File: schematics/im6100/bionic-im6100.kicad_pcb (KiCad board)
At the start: 2 copper layers, 48.3 x 71.1 mm, 10 parts, among them J1 Bionic-P135, J2 Bionic-P245, U1 IM6100, U2 74HCT126, U3 11AA010-I/TO

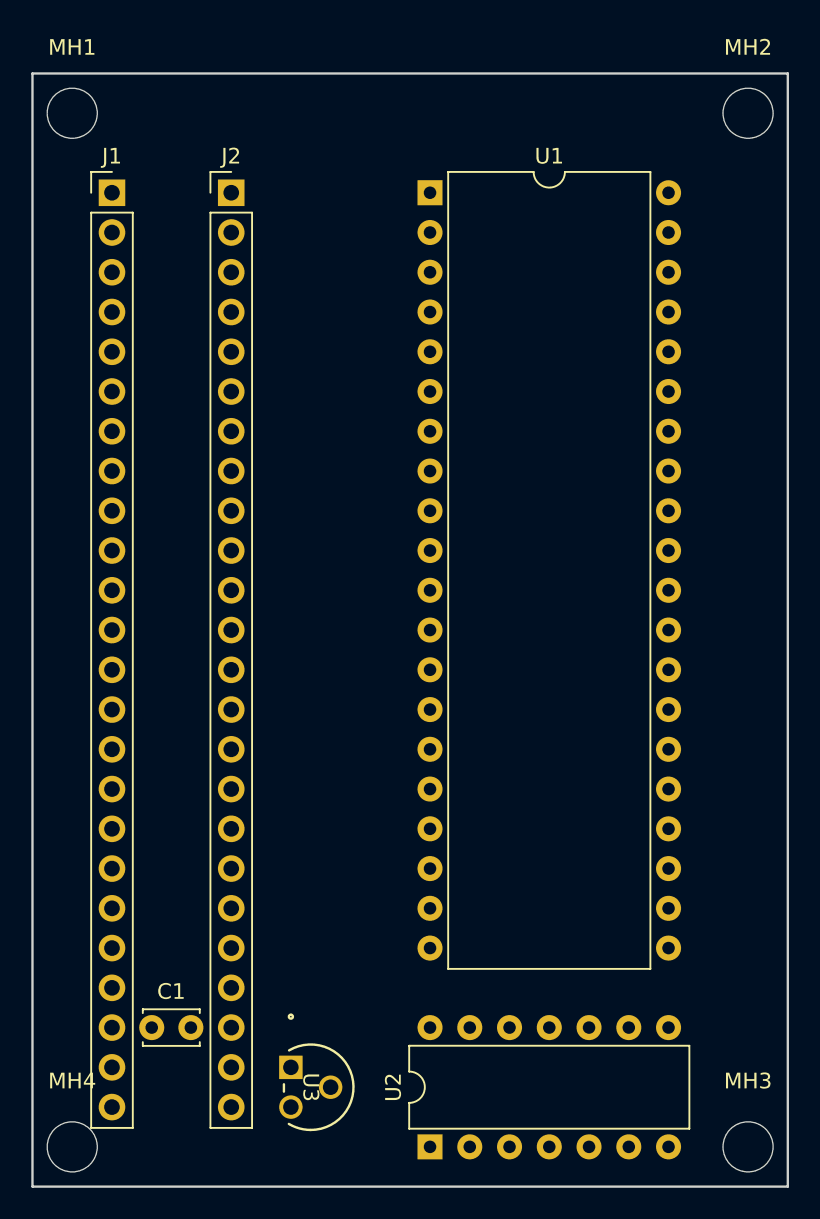
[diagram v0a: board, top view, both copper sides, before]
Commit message: [IM6100] Update schematics
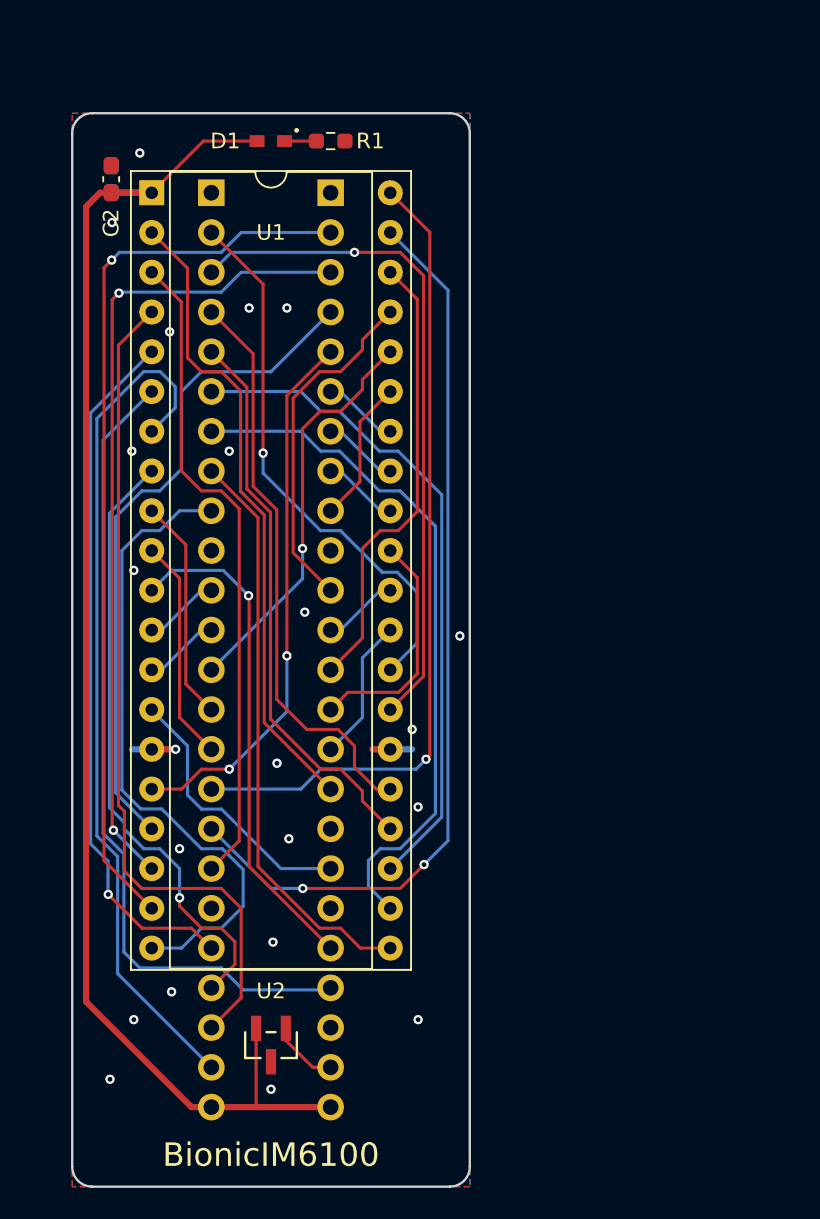
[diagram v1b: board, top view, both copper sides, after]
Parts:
- removed MH1, MH2, MH3, MH4: MountingHole_3.2mm_M3, MountingHole:MountingHole_3.2mm_M3
- removed U3: 11AA010-I/TO, microchip:TO-92_MC_MCH
- added C2: 22u, Capacitor_SMD:C_0603_1608Metric_Pad1.08x0.95mm_HandSolder, F.Cu at (103.5, 74.2)
- added D1: CSL1901UW1, 0-LocalLibrary:LED_CSL1901UW1_ROM-M, F.Cu at (113.7, 71.8)
- added R1: 1.6k, Resistor_SMD:R_0603_1608Metric_Pad0.98x0.95mm_HandSolder, F.Cu at (117.5, 71.8)
- C1: footprint Capacitor_THT:C_Disc_D3.4mm_W2.1mm_P2.50mm -> Capacitor_SMD:C_0603_1608Metric_Pad1.08x0.95mm_HandSolder; moved to B.Cu
- J1: footprint connector:Bionic-P135_Vertical -> 0-LocalLibrary:Bionic-P135_Vertical; moved to B.Cu
- J2: footprint connector:Bionic-P245_Vertical -> 0-LocalLibrary:Bionic-P245_Vertical; moved to B.Cu
- U1: footprint Package_DIP:DIP-40_W15.24mm -> 0-LocalLibrary:DIP-40_W15.24mm_Socket
- U2: value 74HCT126 -> 11AA010-I/TT; footprint Package_DIP:DIP-14_W7.62mm -> 0-LocalLibrary:SOT-23_MC_MCH-M
- moved C1 54.3 mm to (103.5, 74.2), turned to 90 degrees
- moved U1 17.8 mm to (106.1, 75.1)
- moved U2 12.1 mm to (113.7, 129.5), turned to 180 degrees
- moved J2 6.35 mm to (117.5, 75.1), turned to 180 degrees
- moved J1 6.35 mm to (109.9, 75.1), turned to 180 degrees
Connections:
- J1 pad 14: unconnected-(J1-P33-Pad14) -> /P33
- J2 pad 32: /P46 -> unconnected-(J2-P46-Pad32)
- U1 pad 10: /P40 -> /P34
- U1 pad 11: /P52 -> /P54
- U1 pad 12: /P31 -> /P30
- U1 pad 13: /P32 -> /P31
- U1 pad 14: Net-(U1-OSCOUT) -> /P47
- U1 pad 3: /P36 -> /P37
- U1 pad 30: /P47 -> /P41
- U1 pad 31: /P34 -> /P43
- U1 pad 36: /P51 -> /P32
- U1 pad 37: /P55 -> /P40
- U1 pad 38: /P35 -> /P42
- U1 pad 39: /P54 -> /P36
- U1 pad 4: /P37 -> /P52
- U1 pad 40: /P50 -> /P35
- U1 pad 5: /P42 -> /P50
- U1 pad 6: /P41 -> /P55
- U1 pad 8: /P43 -> /P51
- U1 pad 9: /P30 -> /P33
- U2 pad 1: VCC -> Net-(J2-P57)
- U2 pad 2: /P46 -> VCC
- U2 pad 3: Net-(U1-OSCOUT) -> GND
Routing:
- net VCC: track 0.00 -> 89.5 mm
- net /P36: track 0.00 -> 58.3 mm, vias 0 -> 2
- net /P20: track 0.00 -> 57.6 mm, vias 0 -> 1
- net /P53: track 0.00 -> 54.6 mm
- net /P52: track 0.00 -> 53.6 mm
- net /P21: track 0.00 -> 52.1 mm, vias 0 -> 2
- net /P55: track 0.00 -> 51.9 mm
- net /P35: track 0.00 -> 51.8 mm, vias 0 -> 1
- net /P50: track 0.00 -> 44.8 mm, vias 0 -> 1
- net /P15: track 0.00 -> 44.3 mm
- net /P11: track 0.00 -> 43.3 mm, vias 0 -> 1
- net /P22: track 0.00 -> 42.9 mm
- net /P14: track 0.00 -> 42.7 mm
- net /P37: track 0.00 -> 41.9 mm
- net /P17: track 0.00 -> 41.2 mm
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- added copper zone on B.Cu, net GND
- added copper zone on F.Cu, net GND
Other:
- board size 48.3 x 71.1 mm -> 25.4 x 68.6 mm
- board text added: "BionicIM6100"
- board text added: "JLCJLCJLCJLC"
- board text added: "Rev. 2"

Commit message: [IM6100] Cleanup schematics
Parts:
- D1: footprint 0-LocalLibrary:LED_CSL1901UW1_ROM-M -> rhom:LED_CSL1901UW1_ROM-M
- J1: footprint 0-LocalLibrary:Bionic-P135_Vertical -> bionic:Bionic-P135_Vertical
- J2: footprint 0-LocalLibrary:Bionic-P245_Vertical -> bionic:Bionic-P245_Vertical
- U1: footprint 0-LocalLibrary:DIP-40_W15.24mm_Socket -> bionic:DIP-40_W15.24mm_Socket
- U2: footprint 0-LocalLibrary:SOT-23_MC_MCH-M -> microchip:SOT-23_MC_MCH-M
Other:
- rule pad_to_mask_clearance: 0.051 -> 0
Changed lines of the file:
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@@
 			(dielectric_constraints no)
 		)
-		(pad_to_mask_clearance 0.051)
-		(solder_mask_min_width 0.25)
+		(pad_to_mask_clearance 0)
 		(allow_soldermask_bridges_in_footprints no)
 		(aux_axis_origin 101 70)
@@
 	(net 46 "/P33")
 	(net 47 "unconnected-(J2-P46-Pad32)")
-	(footprint "0-LocalLibrary:SOT-23_MC_MCH-M"
+	(footprint "microchip:SOT-23_MC_MCH-M"
 		(locked yes)
 		(layer "F.Cu")
@@
 		(descr "Microchip 11AAxxx-I/TT UNI/O 1Kbit Serial EEPROM")
 		(property "Reference" "U2"
-			(at 0 3.4544 0)
+			(at 0 3.0988 0)
 			(unlocked yes)
 			(layer "F.SilkS")
@@
 			)
 		)
-		(property "Footprint" "0-LocalLibrary:SOT-23_MC_MCH-M"
+		(property "Footprint" "microchip:SOT-23_MC_MCH-M"
 			(at 0 0 180)
 			(layer "F.Fab")
@@
 			)
 		)
-		(property "Description" ""
+		(property "Description" "UNI/O Serial EEPROM (1Kbit)"
 			(at 0 0 180)
 			(layer "F.Fab")
@@
 			(pintype "power_in")
 		)
-		(model "${KIPRJMOD}/0-LocalLibrary/SOT-23_MC_MCH.step"
+		(model "${KIPRJMOD}/microchip.pretty/SOT-23_MC_MCH.step"
 			(offset
 				(xyz 0 0 0)
@@
 		)
 	)
-	(footprint "0-LocalLibrary:LED_CSL1901UW1_ROM-M"
+	(footprint "rhom:LED_CSL1901UW1_ROM-M"
 		(layer "F.Cu")
 		(at 113.6873 71.778 180)
@@
 		(tags "CSL1901UW1 ")
 		(property "Reference" "D1"
-			(at 2.9083 0 0)
+			(at 2.8829 0 0)
 			(unlocked yes)
 			(layer "F.SilkS")
@@
 			)
 		)
-		(property "Footprint" "0-LocalLibrary:LED_CSL1901UW1_ROM-M"
-			(at 0 0 360)
+		(property "Footprint" "rhom:LED_CSL1901UW1_ROM-M"
+			(at 0 0 180)
 			(layer "F.Fab")
 			(hide yes)
@@
 		)
 		(property "Datasheet" "https://fscdn.rohm.com/en/products/databook/datasheet/opto/led/chip_mono/csl1901uw1-e.pdf"
-			(at 0 0 360)
+			(at 0 0 180)
 			(layer "F.Fab")
 			(hide yes)
@@
 		)
 		(property "Description" "Red LED (Low Current Emission, SMD)"
-			(at 0 0 360)
+			(at 0 0 180)
 			(layer "F.Fab")
 			(hide yes)
@@
 			)
 		)
-		(model "${KIPRJMOD}/0-LocalLibrary/LED_CSL1901UW1_ROM.step"
+		(model "${KIPRJMOD}/rhom.pretty/LED_CSL1901UW1_ROM.step"
 			(offset
 				(xyz 0 0 0)
@@
 		)
 	)
-	(footprint "0-LocalLibrary:DIP-40_W15.24mm_Socket"
+	(footprint "bionic:DIP-40_W15.24mm_Socket"
 		(locked yes)
 		(layer "F.Cu")
@@
 		(tags "THT DIP DIL PDIP 2.54mm 15.24mm 600mil Socket")
 		(property "Reference" "U1"
-			(at 7.62 2.54 0)
+			(at 7.62 2.3876 0)
 			(layer "F.SilkS")
 			(effects
@@
 			)
 		)
-		(property "Footprint" "0-LocalLibrary:DIP-40_W15.24mm_Socket"
+		(property "Footprint" "bionic:DIP-40_W15.24mm_Socket"
 			(at 0 0 0)
 			(layer "F.Fab")
@@
 		)
 	)
-	(footprint "0-LocalLibrary:Bionic-P245_Vertical"
+	(footprint "bionic:Bionic-P245_Vertical"
 		(locked yes)
 		(layer "B.Cu")
@@
 			)
 		)
-		(property "Footprint" "0-LocalLibrary:Bionic-P245_Vertical"
-			(at 0 0 180)
-			(layer "F.Fab")
+		(property "Footprint" "bionic:Bionic-P245_Vertical"
+			(at 0 0 0)
+			(layer "B.Fab")
 			(hide yes)
 			(effects
@@
 					(thickness 0.15)
 				)
+				(justify mirror)
 			)
 		)
 		(property "Datasheet" ""
-			(at 0 0 180)
-			(layer "F.Fab")
+			(at 0 0 0)
+			(layer "B.Fab")
 			(hide yes)
 			(effects
@@
 					(thickness 0.15)
 				)
-			)
-		)
-		(property "Description" ""
-			(at 0 0 180)
-			(layer "F.Fab")
+				(justify mirror)
+			)
+		)
+		(property "Description" "Generic connector, single row, 01x24, script generated (kicad-library-utils/schlib/autogen/connector/)"
+			(at 0 0 0)
+			(layer "B.Fab")
 			(hide yes)
 			(effects
@@
 					(thickness 0.15)
 				)
+				(justify mirror)
 			)
 		)
@@
 		)
 	)
-	(footprint "0-LocalLibrary:Bionic-P135_Vertical"
+	(footprint "bionic:Bionic-P135_Vertical"
 		(locked yes)
 		(layer "B.Cu")
@@
 			)
 		)
-		(property "Footprint" "0-LocalLibrary:Bionic-P135_Vertical"
-			(at 0 0 180)
-			(layer "F.Fab")
+		(property "Footprint" "bionic:Bionic-P135_Vertical"
+			(at 0 0 0)
+			(layer "B.Fab")
 			(hide yes)
 			(effects
@@
 					(thickness 0.15)
 				)
+				(justify mirror)
 			)
 		)
 		(property "Datasheet" ""
-			(at 0 0 180)
-			(layer "F.Fab")
+			(at 0 0 0)
+			(layer "B.Fab")
 			(hide yes)
 			(effects
@@
 					(thickness 0.15)
 				)
-			)
-		)
-		(property "Description" ""
-			(at 0 0 180)
-			(layer "F.Fab")
+				(justify mirror)
+			)
+		)
+		(property "Description" "Generic connector, single row, 01x24, script generated (kicad-library-utils/schlib/autogen/connector/)"
+			(at 0 0 0)
+			(layer "B.Fab")
 			(hide yes)
 			(effects
@@
 					(thickness 0.15)
 				)
-			)
-		)
+				(justify mirror)
+			)
+		)

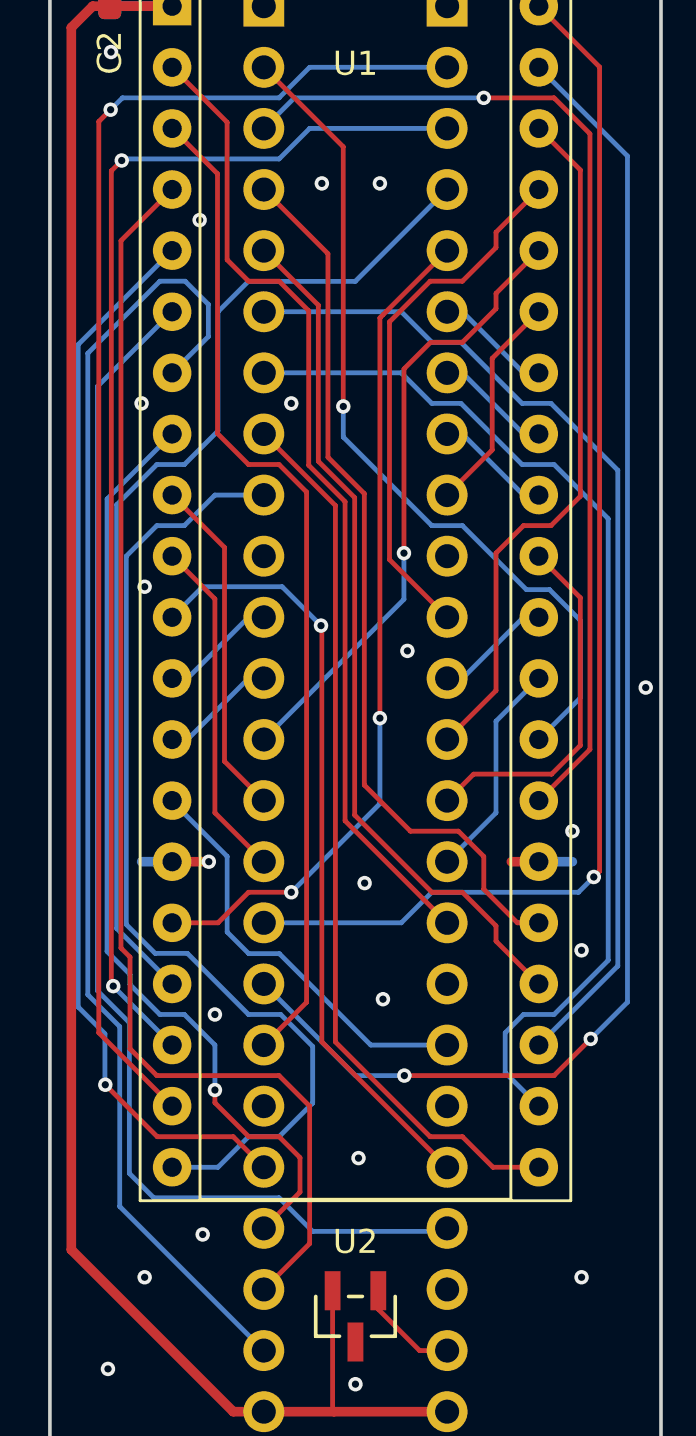
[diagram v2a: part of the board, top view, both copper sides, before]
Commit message: [IM6100] Update schematics
Remove unused pins from bionic connector
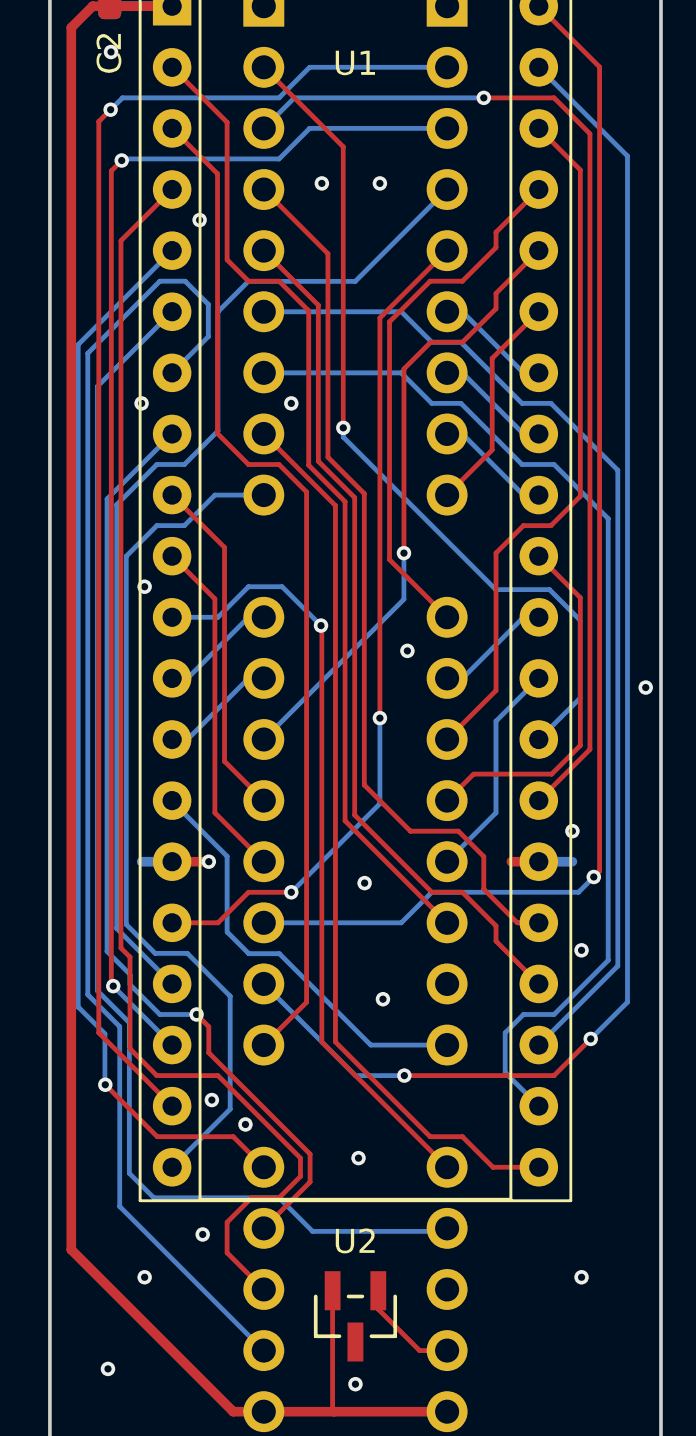
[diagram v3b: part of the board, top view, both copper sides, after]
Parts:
- J1: footprint bionic:Bionic-P135_Vertical -> bionic:Bionic-P135_THT
- J2: footprint bionic:Bionic-P245_Vertical -> bionic:Bionic-P245_THT
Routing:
- net /P17: track 41.2 -> 35.7 mm
- net GND: vias 22 -> 23
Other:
- board text added: "Rev. 3"
- board text removed: "Rev. 2"
